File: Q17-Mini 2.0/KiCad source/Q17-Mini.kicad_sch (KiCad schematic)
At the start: 83 parts, among them J1 INPUT, J2-1 SPK+, J2-2 SPK-, J3-1 V+, J3-2 GND, J3-3 V-, Q1 IRF610, Q10 KSA992, Q12 KSC1845, Q13 IRF610, Q14 IRF9610, Q15 FQA46N15, Q16 IXTH48P20P, Q2 KSA992, Q3 KSC1845, Q4 IRF9610, Q5 FQPF7P20, Q6 2SK3564, Q7 LSK170B, Q8 DN2540, Q9 BS250P, U1 OPA1611, U2 NDC7003P

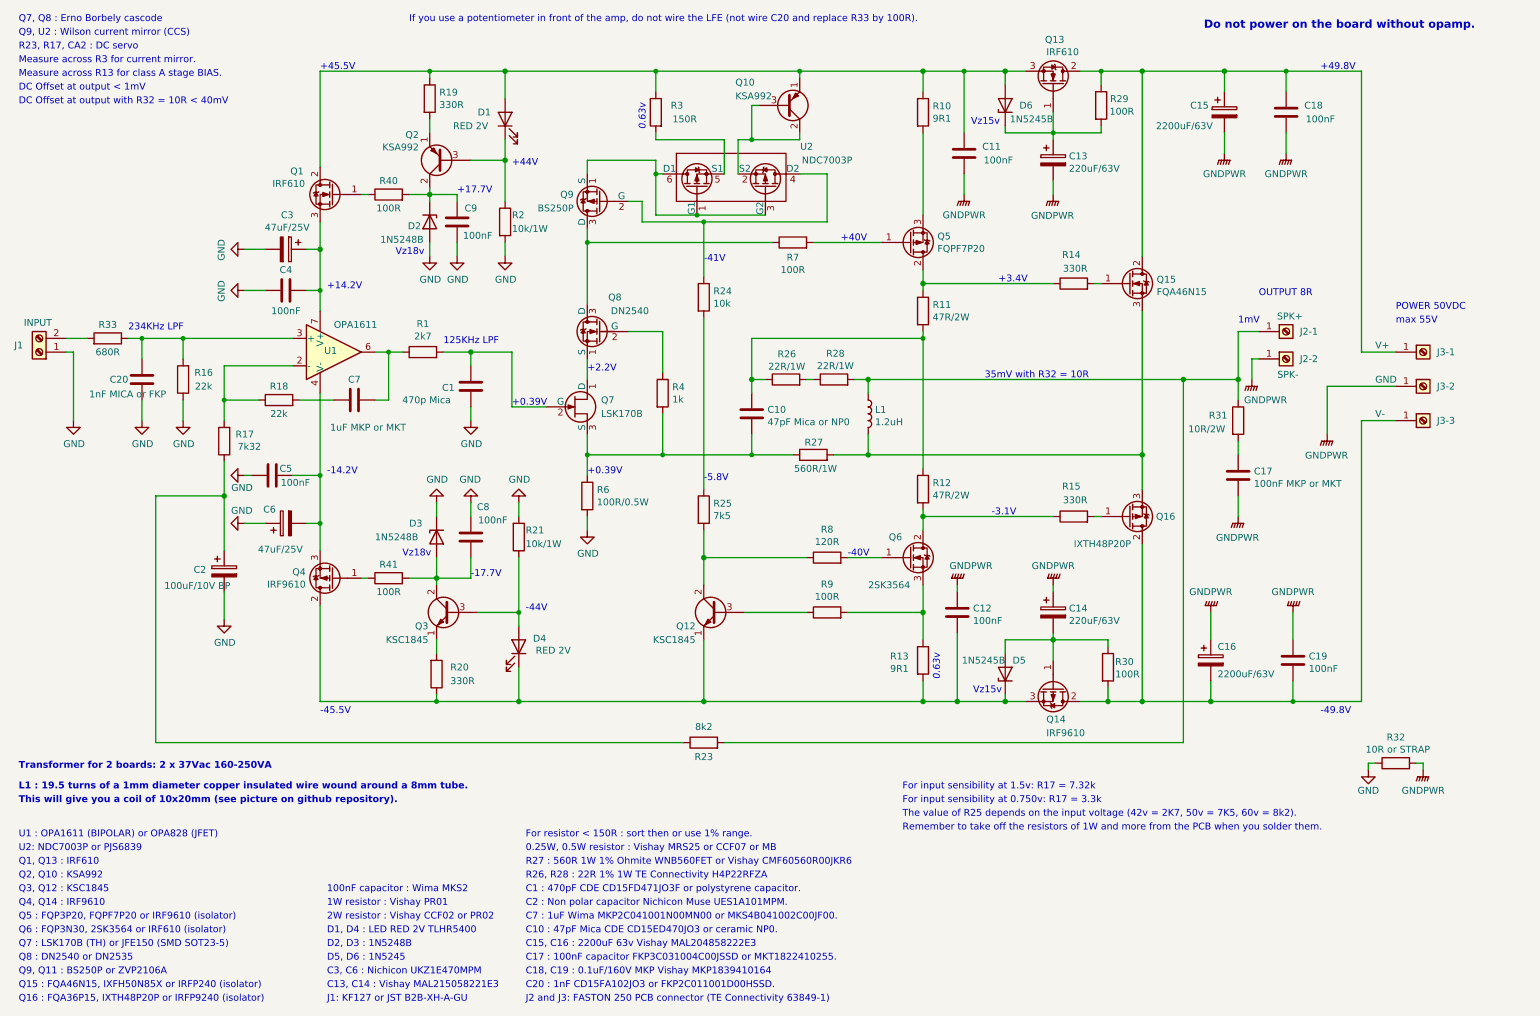
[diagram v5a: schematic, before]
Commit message: Update measures on Q17-Mini 2.0
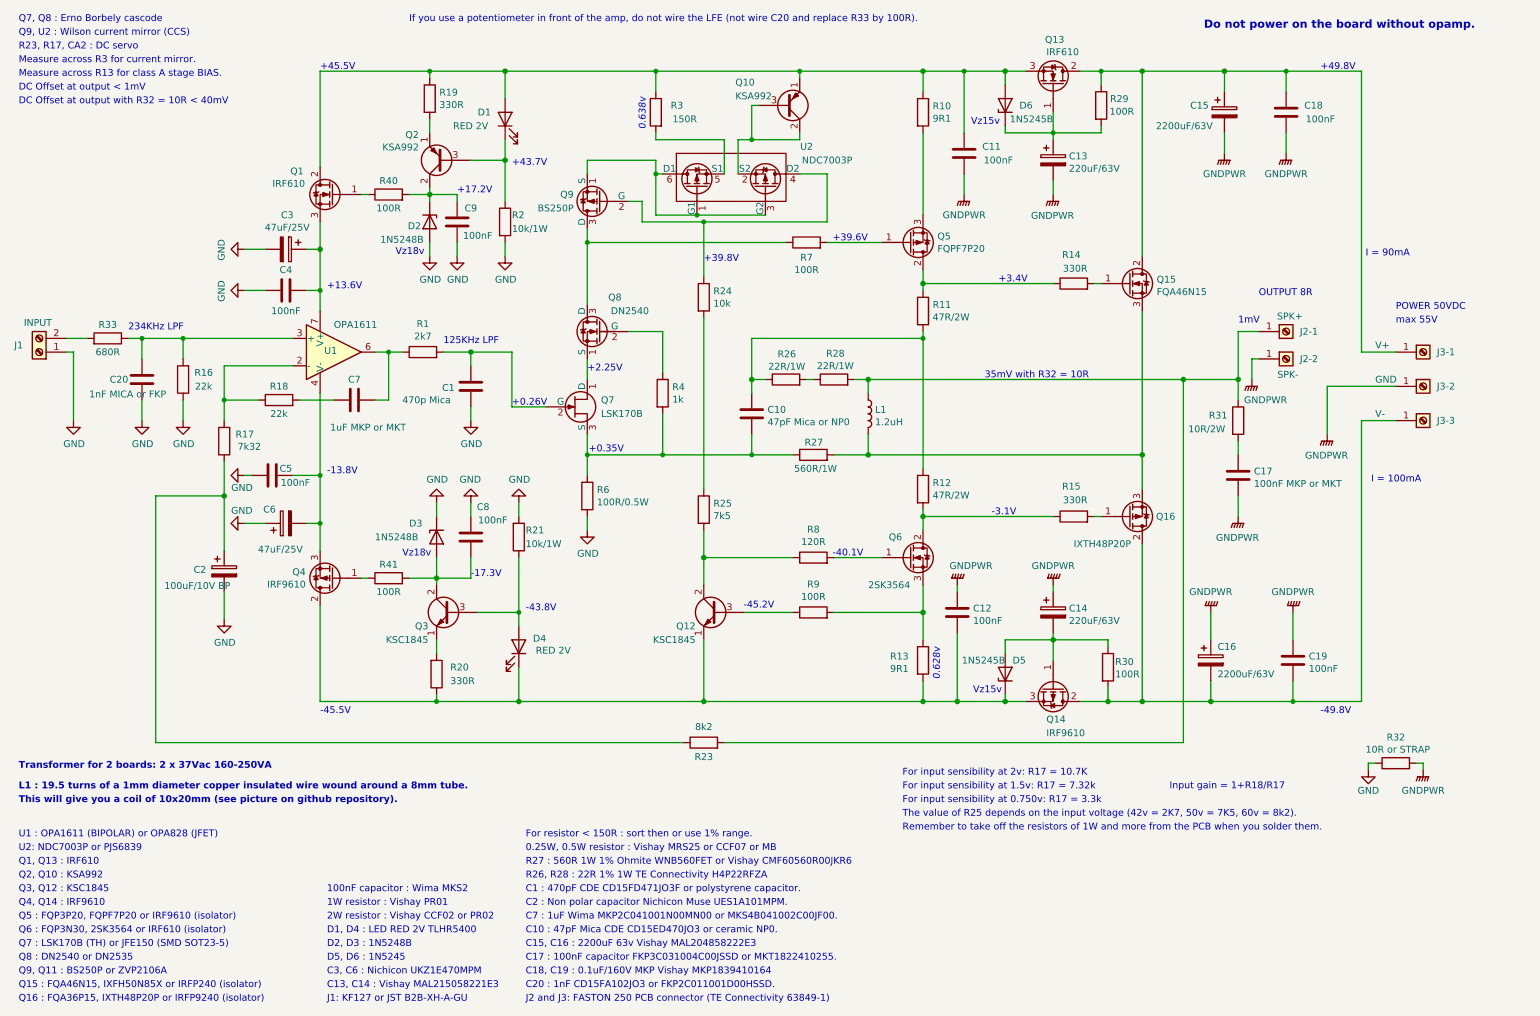
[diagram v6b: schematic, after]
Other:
- note added: "+0.26V"
- note added: "+0.35V"
- note added: "+13.6V"
- note added: "+17.2V"
- note added: "+2.25V"
- note added: "+39.6V"
- note added: "+39.8V"
- note added: "+43.7V"
- note added: "-13.8V"
- note added: "-17.3V"
- note added: "-40.1V"
- note added: "-43.8V"
- note added: "-45.2V"
- note added: "0.628v"
- note added: "0.638v"
- note added: "For input sensibility at 2v: R17 = 10.7K"
- note added: "I = 100mA"
- note added: "I = 90mA"
- note added: "Input gain = 1+R18/R17"
- note removed: "+0.39V"
- note removed: "+14.2V"
- note removed: "+17.7V"
- note removed: "+2.2V"
- note removed: "+40V"
- note removed: "+44V"
- note removed: "-14.2V"
- note removed: "-17.7V"
- note removed: "-40V"
- note removed: "-41V"
- note removed: "-44V"
- note removed: "-5.8V"
- note removed: "0.63v"
- moved on the sheet: R7, R8, R9
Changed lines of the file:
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@@
 	(title_block
 		(title "Q17-Mini Amplifier 2.x")
-		(date "2024-04-30")
-		(rev "2.0.5")
+		(date "2024-05-12")
+		(rev "2.0.6")
 		(company "by eng. Tiberiu Vicol")
 		(comment 1 "Modified by Stef for the Q17-Mini project")
@@
 	(wire
 		(pts
-			(xy 173.99 55.88) (xy 161.29 55.88)
+			(xy 173.99 55.88) (xy 163.83 55.88)
 		)
 		(stroke
@@
 	(wire
 		(pts
-			(xy 167.64 114.3) (xy 173.99 114.3)
+			(xy 165.1 114.3) (xy 173.99 114.3)
 		)
 		(stroke
@@
 	(wire
 		(pts
-			(xy 140.97 114.3) (xy 160.02 114.3)
+			(xy 140.97 114.3) (xy 157.48 114.3)
 		)
 		(stroke
@@
 	(wire
 		(pts
-			(xy 167.64 124.46) (xy 181.61 124.46)
+			(xy 165.1 124.46) (xy 181.61 124.46)
 		)
 		(stroke
@@
 	(wire
 		(pts
-			(xy 148.59 124.46) (xy 160.02 124.46)
+			(xy 148.59 124.46) (xy 157.48 124.46)
 		)
 		(stroke
@@
 	(wire
 		(pts
-			(xy 119.38 55.88) (xy 153.67 55.88)
+			(xy 119.38 55.88) (xy 156.21 55.88)
 		)
 		(stroke
@@
 		)
 	)
-	(text "-44V"
+	(text "-43.8V"
 		(exclude_from_sim no)
 		(at 107.95 124.46 0)
@@
 		)
 	)
-	(text "+2.2V"
+	(text "+2.25V"
 		(exclude_from_sim no)
 		(at 119.38 80.01 0)
@@
 		)
 	)
-	(text "-17.7V"
+	(text "-17.3V"
 		(exclude_from_sim no)
 		(at 97.79 118.11 0)
@@
 		)
 	)
-	(text "+0.39V"
+	(text "+0.35V"
 		(exclude_from_sim no)
-		(at 119.38 99.06 0)
+		(at 119.634 94.996 0)
 		(effects
 			(font
@@
 		)
 	)
+	(text "Input gain = 1+R18/R17"
+		(exclude_from_sim no)
+		(at 237.998 156.718 0)
+		(effects
+			(font
+				(size 1.27 1.27)
+			)
+		)
+	)
 	(text "Q1, Q13 : IRF610"
 		(exclude_from_sim no)
@@
 		)
 	)
-	(text "J1: KF127 or JST B2B-XH-A-GU"
+	(text "I = 90mA"
 		(exclude_from_sim no)
-		(at 71.12 196.85 0)
+		(at 263.652 58.674 0)
 		(effects
 			(font
 				(size 1.27 1.27)
+				(color 255 3 20 1)
 			)
 			(justify left bottom)
 		)
 	)
-	(text "U1 : OPA1611 (BIPOLAR) or OPA828 (JFET)"
+	(text "J1: KF127 or JST B2B-XH-A-GU"
 		(exclude_from_sim no)
-		(at 13.97 166.37 0)
+		(at 71.12 196.85 0)
 		(effects
 			(font
@@
 		)
 	)
-	(text "-5.8V"
+	(text "U1 : OPA1611 (BIPOLAR) or OPA828 (JFET)"
 		(exclude_from_sim no)
-		(at 140.97 100.33 0)
+		(at 13.97 166.37 0)
 		(effects
 			(font
 				(size 1.27 1.27)
-				(color 255 3 20 1)
 			)
 			(justify left bottom)
@@
 		)
 	)
+	(text "For input sensibility at 2v: R17 = 10.7K"
+		(exclude_from_sim no)
+		(at 177.8 154.94 0)
+		(effects
+			(font
+				(size 1.27 1.27)
+			)
+			(justify left bottom)
+		)
+	)
 	(text "Q6 : FQP3N30, 2SK3564 or IRF610 (isolator)"
 		(exclude_from_sim no)
@@
 		)
 	)
-	(text "0.63v"
+	(text "0.638v"
 		(exclude_from_sim no)
 		(at 130.3215 35.1112 90)
@@
 		)
 	)
-	(text "+14.2V"
+	(text "+13.6V"
 		(exclude_from_sim no)
 		(at 71.12 64.77 0)
@@
 		)
 	)
+	(text "I = 100mA"
+		(exclude_from_sim no)
+		(at 264.668 100.584 0)
+		(effects
+			(font
+				(size 1.27 1.27)
+				(color 255 3 20 1)
+			)
+			(justify left bottom)
+		)
+	)
 	(text "2W resistor : Vishay CCF02 or PR02"
 		(exclude_from_sim no)
@@
 		)
 	)
-	(text "-14.2V"
+	(text "-13.8V"
 		(exclude_from_sim no)
 		(at 71.12 99.06 0)
@@
 		)
 	)
-	(text "+40V"
+	(text "+39.6V"
 		(exclude_from_sim no)
-		(at 166.37 55.88 0)
+		(at 164.846 55.88 0)
 		(effects
 			(font
@@
 		)
 	)
-	(text "+0.39V"
+	(text "+0.26V"
 		(exclude_from_sim no)
 		(at 105.41 86.36 0)
@@
 		)
 	)
-	(text "+44V"
+	(text "+43.7V"
 		(exclude_from_sim no)
 		(at 105.41 41.91 0)
@@
 		)
 	)
+	(text "-45.2V"
+		(exclude_from_sim no)
+		(at 148.336 123.952 0)
+		(effects
+			(font
+				(size 1.27 1.27)
+				(color 255 3 20 1)
+			)
+			(justify left bottom)
+		)
+	)
 	(text "Vz15v"
 		(exclude_from_sim no)
@@
 		)
 	)
-	(text "-40V"
+	(text "-40.1V"
 		(exclude_from_sim no)
-		(at 167.64 114.3 0)
+		(at 164.846 114.3 0)
 		(effects
 			(font
@@
 		)
 	)
-	(text "0.63v"
+	(text "0.628v"
 		(exclude_from_sim no)
 		(at 184.8687 137.0676 90)
@@
 		)
 	)
-	(text "-41V"
+	(text "+39.8V"
 		(exclude_from_sim no)
 		(at 140.97 59.69 0)
@@
 		)
 	)
-	(text "+17.7V"
+	(text "+17.2V"
 		(exclude_from_sim no)
 		(at 95.25 46.99 0)
@@
 	(symbol
 		(lib_id "Device:R")
-		(at 163.83 124.46 90)
+		(at 161.29 124.46 90)
 		(unit 1)
 		(exclude_from_sim no)
@@
 		(dnp no)
 		(property "Reference" "R9"
-			(at 163.83 119.2338 90)
+			(at 161.29 119.2338 90)
 			(effects
 				(font
@@
 		)
 		(property "Value" "100R"
-			(at 163.83 121.533 90)
+			(at 161.29 121.533 90)
 			(effects
 				(font
@@
 		)
 		(property "Footprint" "Resistor_THT:R_Axial_DIN0207_L6.3mm_D2.5mm_P10.16mm_Horizontal"
-			(at 163.83 126.238 90)
+			(at 161.29 126.238 90)
 			(effects
 				(font
@@
 		)
 		(property "Datasheet" "https://www.vishay.com/doc?28724"
-			(at 163.83 124.46 0)
+			(at 161.29 124.46 0)
 			(effects
 				(font
@@
 		)
 		(property "Description" ""
-			(at 163.83 124.46 0)
+			(at 161.29 124.46 0)
 			(effects
 				(font
@@
 		)
 		(property "Part#" "MRS25000C1000FCT00"
-			(at 163.83 124.46 90)
+			(at 161.29 124.46 90)
 			(effects
 				(font
@@
 		)
 		(property "Mouser" "594-MRS25000C1000FCT"
-			(at 163.83 124.46 90)
+			(at 161.29 124.46 90)
 			(effects
 				(font
@@
 	(symbol
 		(lib_id "Device:R")
-		(at 157.48 55.88 90)
+		(at 160.02 55.88 90)
 		(unit 1)
 		(exclude_from_sim no)
@@
 		(dnp no)
 		(property "Reference" "R7"
-			(at 157.48 58.6613 90)
+			(at 160.02 58.6613 90)
 			(effects
 				(font
@@
 		)
 		(property "Value" "100R"
-			(at 157.48 60.96 90)
+			(at 160.02 60.96 90)
 			(effects
 				(font
@@
 		)
 		(property "Footprint" "Resistor_THT:R_Axial_DIN0207_L6.3mm_D2.5mm_P10.16mm_Horizontal"
-			(at 157.48 57.658 90)
+			(at 160.02 57.658 90)
 			(effects
 				(font
@@
 		)
 		(property "Datasheet" "https://www.vishay.com/doc?28724"
-			(at 157.48 55.88 0)
+			(at 160.02 55.88 0)
 			(effects
 				(font
@@
 		)
 		(property "Description" ""
-			(at 157.48 55.88 0)
+			(at 160.02 55.88 0)
 			(effects
 				(font
@@
 		)
 		(property "Part#" "MRS25000C1000FCT00"
-			(at 157.48 55.88 90)
+			(at 160.02 55.88 90)
 			(effects
 				(font
@@
 		)
 		(property "Mouser" "594-MRS25000C1000FCT"
-			(at 157.48 55.88 90)
+			(at 160.02 55.88 90)
 			(effects
 				(font
@@
 	(symbol
 		(lib_id "Device:R")
-		(at 163.83 114.3 90)
+		(at 161.29 114.3 90)
 		(unit 1)
 		(exclude_from_sim no)
@@
 		(dnp no)
 		(property "Reference" "R8"
-			(at 163.83 109.0738 90)
+			(at 161.29 109.0738 90)
 			(effects
 				(font
@@
 		)
 		(property "Value" "120R"
-			(at 163.83 111.3725 90)
+			(at 161.29 111.3725 90)
 			(effects
 				(font
@@
 		)
 		(property "Footprint" "Resistor_THT:R_Axial_DIN0207_L6.3mm_D2.5mm_P10.16mm_Horizontal"
-			(at 163.83 116.078 90)
+			(at 161.29 116.078 90)
 			(effects
 				(font
@@
 		)
 		(property "Datasheet" "https://www.vishay.com/doc?28724"
-			(at 163.83 114.3 0)
+			(at 161.29 114.3 0)
 			(effects
 				(font
@@
 		)
 		(property "Description" ""
-			(at 163.83 114.3 0)
+			(at 161.29 114.3 0)
 			(effects
 				(font
@@
 		)
 		(property "Part#" "MRS25000C1200FCT00"
-			(at 163.83 114.3 90)
+			(at 161.29 114.3 90)
 			(effects
 				(font
@@
 		)
 		(property "Mouser" "594-MRS25000C1200FCT"
-			(at 163.83 114.3 90)
+			(at 161.29 114.3 90)
 			(effects
 				(font

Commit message: Update Q17-Mini to 2.0.1
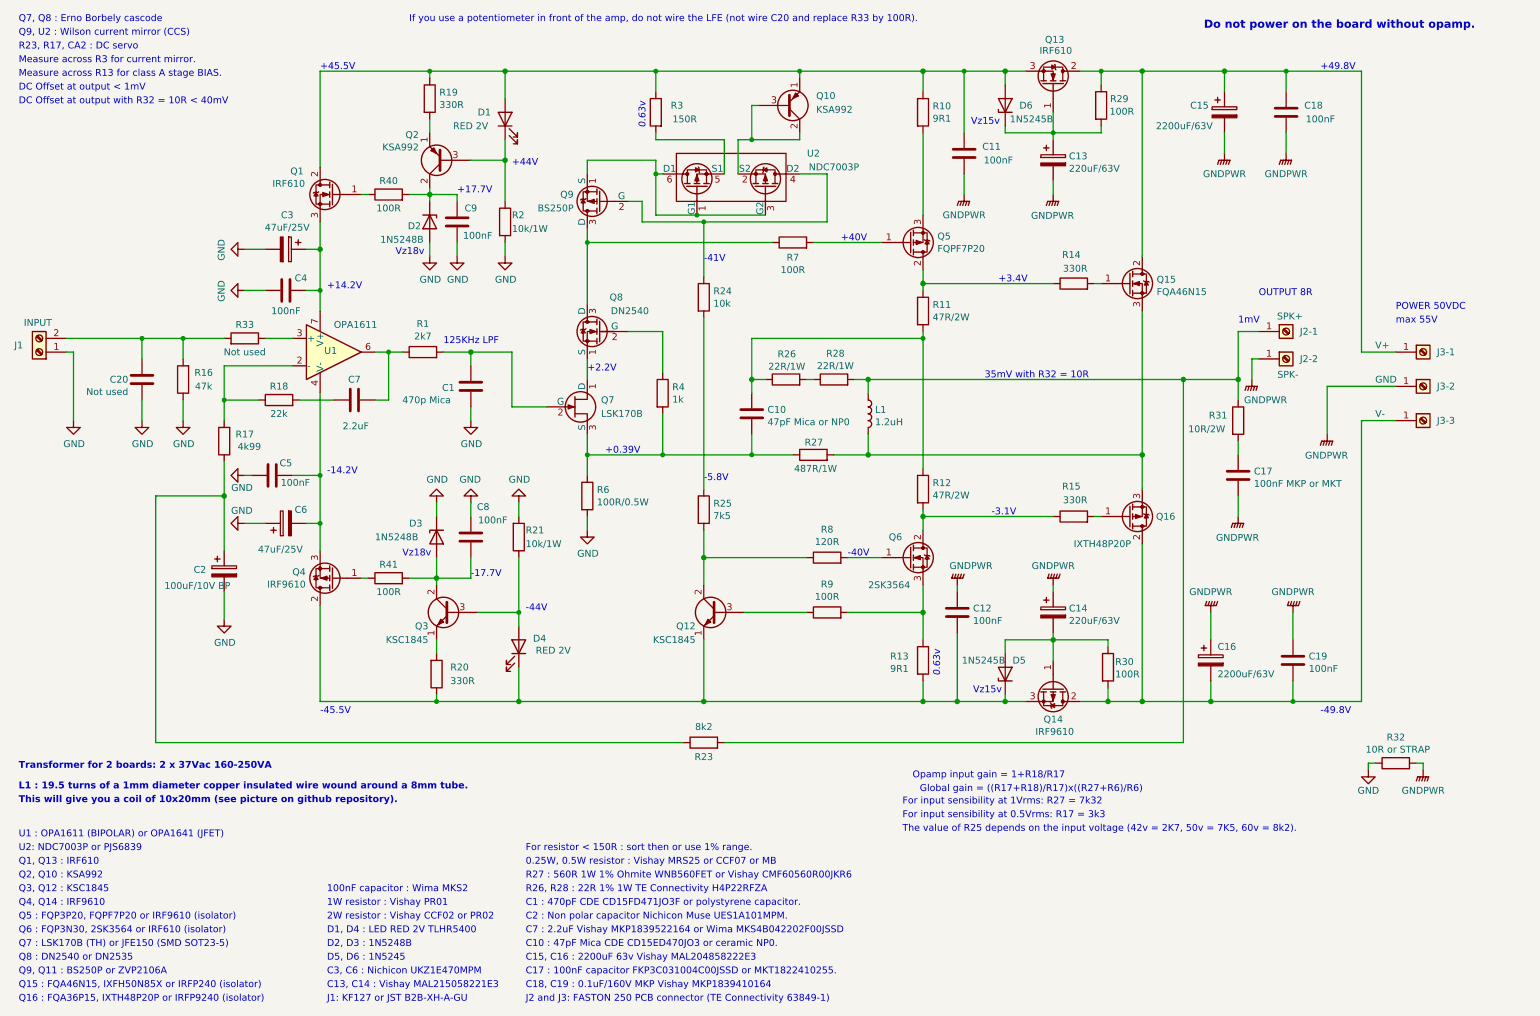
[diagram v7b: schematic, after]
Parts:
- C20: value 1nF MICA or FKP -> Not used; Mouser 598-CD15FA102JO3 -> (none); Part# CD15FA102JO3 -> (none)
- C7: value 1uF MKP or MKT -> 2.2uF; Mouser 505-MKP2C0411NMN -> 75-MKP1839522164; Part# MKP2C041001N00MN00 -> MKP1839522164
- R16: value 22k -> 47k; Mouser 594-MRS25000C2202FCT -> 594-MRS25000C4702FRP; Part# MRS25000C2202FCT00 -> MRS25000C4702FRP00
- R17: value 7k32 -> 4k99; Mouser 660-MF1/4CCT52R7321F -> 594-MRS25000C4991FRP; Part# MF1/4CCT52R7321F -> MRS25000C4991FRP00
- R27: value 560R/1W -> 487R/1W; Mouser 588-WNB560FET -> 279-H4P487RDZA; Part# WNB560FET -> H4P487RDZA
- R33: value 680R -> Not used; Mouser 594-MRS25000C6800FCT -> 594-MRS25000C1009FRP; Part# MRS25000C6800FCT00 -> MRS25000C1009FRP00
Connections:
- net at R33.1, U1.3 (+): no longer C20.2, R16.2
- net at J1.2 (Pin_2), R33.2: now also C20.2, R16.2
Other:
- note added: "+0.39V"
- note added: "+14.2V"
- note added: "+17.7V"
- note added: "+2.2V"
- note added: "+40V"
- note added: "+44V"
- note added: "-14.2V"
- note added: "-17.7V"
- note added: "-40V"
- note added: "-41V"
- note added: "-44V"
- note added: "-5.8V"
- note added: "0.63v"
- note added: "C7 : 2.2uF Vishay MKP1839522164 or Wima MKS4B042202F00JSSD"
- note added: "For input sensibility at 0.5Vrms: R17 = 3k3"
- note added: "For input sensibility at 1Vrms: R27 = 7k32"
- note added: "Global gain = ((R17+R18)/R17)x((R27+R6)/R6)"
- note added: "Opamp input gain = 1+R18/R17"
- note added: "U1 : OPA1611 (BIPOLAR) or OPA1641 (JFET)"
- note removed: "+0.26V"
- note removed: "+0.35V"
- note removed: "+13.6V"
- note removed: "+17.2V"
- note removed: "+2.25V"
- note removed: "+39.6V"
- note removed: "+39.8V"
- note removed: "+43.7V"
- note removed: "-13.8V"
- note removed: "-17.3V"
- note removed: "-40.1V"
- note removed: "-43.8V"
- note removed: "-45.2V"
- note removed: "0.628v"
- note removed: "0.638v"
- note removed: "234KHz LPF"
- note removed: "C20 : 1nF CD15FA102JO3 or FKP2C011001D00HSSD."
- note removed: "C7 : 1uF Wima MKP2C041001N00MN00 or MKS4B041002C00JF00."
- note removed: "For input sensibility at 0.750v: R17 = 3.3k"
- note removed: "For input sensibility at 1.5v: R17 = 7.32k"
- note removed: "For input sensibility at 2v: R17 = 10.7K"
- note removed: "I = 100mA"
- note removed: "I = 90mA"
- note removed: "Input gain = 1+R18/R17"
- note removed: "Remember to take off the resistors of 1W and more from the PCB when you solder them."
- note removed: "U1 : OPA1611 (BIPOLAR) or OPA828 (JFET)"
- moved on the sheet: R33, R7, R8, R9

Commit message: More updates
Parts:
- C7: value 2.2uF -> 2.2uF MKP or FKP
- R17: value 4k99 -> 7k32
- R27: value 487R/1W -> 560R/1W; Mouser 279-H4P487RDZA -> 588-WNB560FET; Part# H4P487RDZA -> WNB560FET
- R33: value Not used -> strap; Mouser 594-MRS25000C1009FRP -> (none); Part# MRS25000C1009FRP00 -> (none)
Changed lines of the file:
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@@
 			)
 		)
-		(property "Value" "Not used"
+		(property "Value" "strap"
 			(at 55.88 76.2 90)
 			(effects
@@
 			)
 		)
-		(property "Datasheet" "https://www.vishay.com/doc?28724"
+		(property "Datasheet" ""
 			(at 55.88 73.66 0)
 			(effects
@@
 			)
 		)
-		(property "Part#" "MRS25000C1009FRP00"
+		(property "Part#" ""
 			(at 55.88 73.66 90)
 			(effects
@@
 			)
 		)
-		(property "Mouser" "594-MRS25000C1009FRP"
+		(property "Mouser" ""
 			(at 55.88 73.66 90)
 			(effects
@@
 			)
 		)
-		(property "Value" "487R/1W"
+		(property "Value" "560R/1W"
 			(at 161.6861 97.8047 90)
 			(effects
@@
 			)
 		)
-		(property "Datasheet" "https://www.mouser.fr/datasheet/2/418/5/ENG_DS_1773230_H-731439.pdf"
+		(property "Datasheet" "https://www.mouser.fr/datasheet/2/303/res_wh_wn-3082550.pdf"
 			(at 161.29 95.25 0)
 			(effects
@@
 			)
 		)
-		(property "Description" "487R resistor"
+		(property "Description" "560R resistor"
 			(at 161.29 95.25 0)
 			(effects
@@
 			)
 		)
-		(property "Part#" "H4P487RDZA"
+		(property "Part#" "WNB560FET"
 			(at 161.29 95.25 90)
 			(effects
@@
 			)
 		)
-		(property "Mouser" "279-H4P487RDZA"
+		(property "Mouser" "588-WNB560FET"
 			(at 161.29 95.25 90)
 			(effects
@@
 			)
 		)
-		(property "Value" "4k99"
+		(property "Value" "7k32"
 			(at 56.7302 93.7195 0)
 			(effects
@@
 			)
 		)
-		(property "Value" "2.2uF"
-			(at 76.454 89.916 90)
+		(property "Value" "2.2uF MKP or FKP"
+			(at 80.01 89.408 90)
 			(effects
 				(font
